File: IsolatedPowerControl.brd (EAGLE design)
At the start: 160 x 100 mm, 38 parts, among them IC1 LM358, K2 G2RATE-OJ, Q1 FDN360P, U1 MCP23008-E/SO, U2 MCP4716A0T-E/CH

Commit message: Initial fit (incomplete routing)
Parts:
- removed D2: P6KEXXCTS-P6KE, diode:DO15-10
- removed K2: G2RATE-OJ, relay:G2RA-SHORTER
- removed LED2: (no value), led:LED5MM
- removed R13: 270, rcl:R0805
- added JP1, JP3, JP6, JP7, JP8: (no value), pinhead:1X01
- JP4: device pinhead:1X07 -> pinhead:1X01
- moved D1 36.7 mm to (2.86, 38.1)
- moved Q1 35.3 mm to (18.7, 45.4), flipped to the bottom, turned to 270 degrees
- moved T3 29.3 mm to (6.35, 44.5), flipped to the bottom
- moved R14 28.4 mm to (22.2, 45.1), flipped to the bottom, turned to 270 degrees
- moved R12 19.4 mm to (12.7, 45.4), flipped to the bottom, turned to 270 degrees
- moved JP4 16.6 mm to (15.6, 36.2), turned to 0 degrees
- moved R11 12.4 mm to (9.84, 43.8), flipped to the bottom, turned to 0 degrees
- moved C6 0.63 mm to (9.53, 39.6)
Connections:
- removed net N$10: JP4.7, K2.S
- removed net N$8: LED2.K, R13.2
- removed net N$9: JP4.6, K2.P
- net DIRECTONOFF_BUFFERED: now also JP7.1; no longer JP4.5
- net N$13: now also JP8.1; no longer JP4.1
- net N$18: now also JP1.1; no longer D2.A, K2.1, R13.1
- net N$3: now also JP3.1; no longer JP4.2
- net V+: no longer D2.C, K2.2, LED2.A
- net VPOWER: now also JP4.1; no longer JP4.3
- net VPOWER_BUFFERED: now also JP6.1; no longer JP4.4
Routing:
- net DIRECTONOFF: track 0.00 -> 15.3 mm
- net V+: track 56.9 -> 69.0 mm
- net N$12: track 0.00 -> 7.44 mm
- net V-: track 12.0 -> 6.93 mm
- net N$3: track 0.00 -> 3.49 mm
- net N$18: track 0.00 -> 3.35 mm
- net FETONOFF: track 0.00 -> 2.95 mm
- net N$13: track 0.00 -> 2.79 mm
- net DIRECTONOFF_BUFFERED: track 0.65 -> 3.32 mm
- net RELAYONOFF: track 0.00 -> 2.47 mm
- net N$7: track 0.00 -> 2.36 mm
- net VPOWER: track 3.51 -> 4.07 mm

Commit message: First layout complete and checked
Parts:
- JP1, JP3, JP4, JP6, JP7, JP8: device pinhead:1X01 -> pinhead:1X01-LARGEPAD
- moved JP6 12.0 mm to (24.1, 45.7), turned to 90 degrees
- moved JP4 11.4 mm to (25.1, 42.5)
- moved C6 6.63 mm to (11.4, 46.0)
- moved R11 6.11 mm to (10.8, 49.8), turned to 90 degrees
- moved IC1 5.72 mm to (10.2, 42.5)
- moved SJ1 5.64 mm to (20.3, 40.0)
- moved T3 5.54 mm to (7.62, 49.8), turned to 270 degrees
- moved C4 5.45 mm to (7.30, 36.2)
- moved JP7 5.40 mm to (5.71, 45.1), turned to 90 degrees
- moved R14 5.40 mm to (24.8, 49.8)
- moved Q1 5.12 mm to (21.3, 49.8)
- moved JP8 4.72 mm to (16.8, 48.9), turned to 90 degrees
- moved R12 4.62 mm to (14.0, 49.8), turned to 315 degrees
- moved C7 4.49 mm to (20.6, 11.9)
- moved JP2 4.49 mm to (14.6, 31.1)
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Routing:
- net VPOWER: track 4.07 -> 17.1 mm
- net VPOWER_BUFFERED: track 0.65 -> 12.9 mm
- net GND: track 9.92 -> 0.34 mm
- net V+: track 69.0 -> 78.2 mm
- net N$12: track 7.44 -> 11.0 mm
- net V-: track 6.93 -> 4.90 mm, vias 1 -> 2
- net N$11: track 2.87 -> 4.74 mm
- net SDA: track 31.1 -> 29.3 mm
- net SCL: track 21.3 -> 22.4 mm
- net N$13: track 2.79 -> 3.74 mm
- net RY-SCL: track 9.94 -> 10.8 mm
- net RELAYONOFF: track 2.47 -> 3.28 mm
- net N$2: track 4.79 -> 4.07 mm
- net DIRECTONOFF: track 15.3 -> 14.7 mm
- net N$5: track 7.95 -> 7.37 mm, vias 2 -> 1
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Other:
- board size 160 x 100 mm -> 27.9 x 53.6 mm

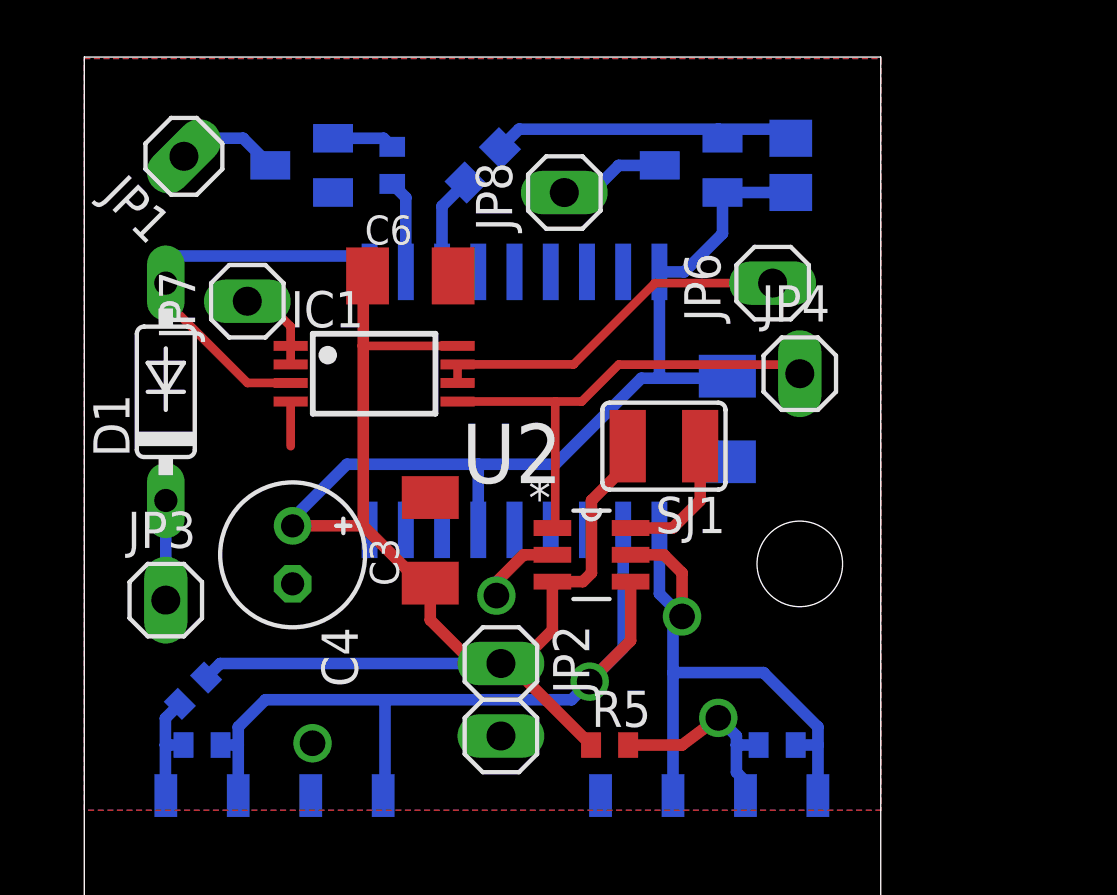
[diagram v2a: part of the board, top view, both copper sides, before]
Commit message: Added op amp with enable/power down (MCP6273T) and re-routed.
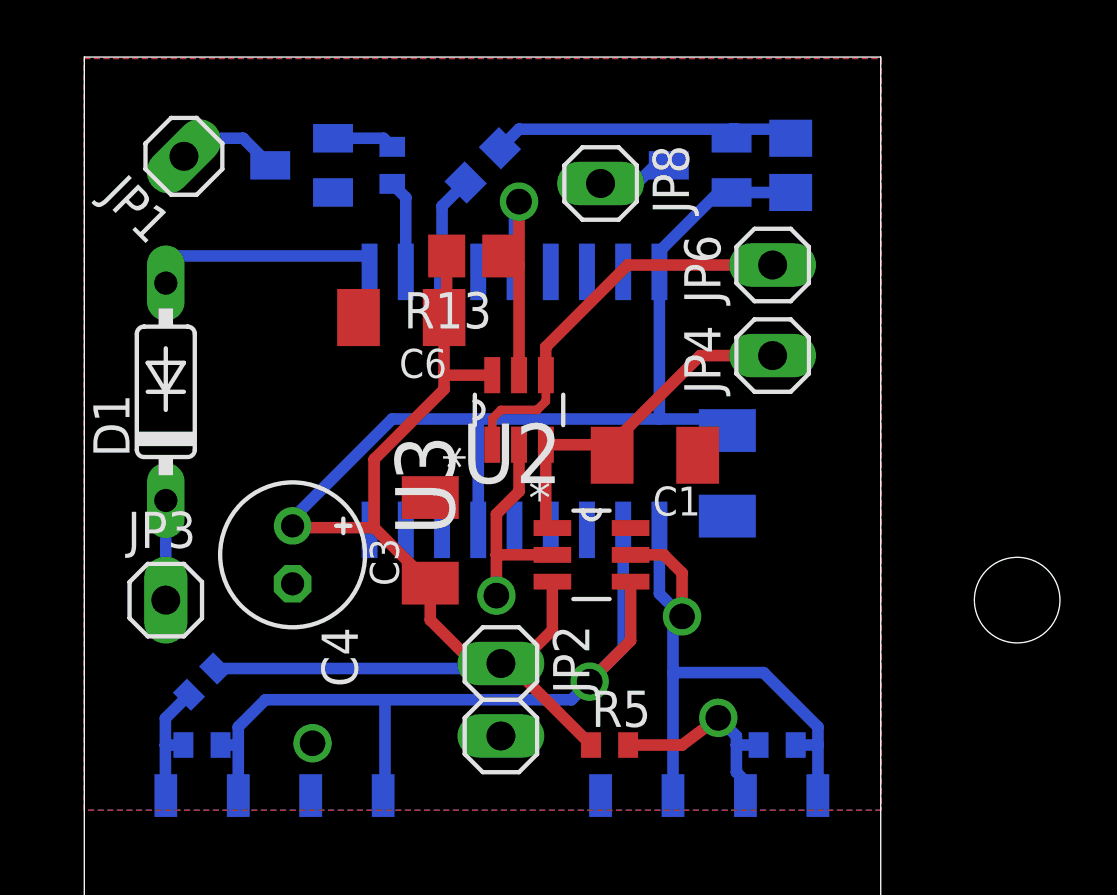
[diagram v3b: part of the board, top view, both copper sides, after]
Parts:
- removed IC1: LM358, linear:TSSOP8
- removed JP7: (no value), pinhead:1X01-LARGEPAD
- removed SJ1: (no value), jumper:SJW
- added C1: 100n, rcl:C1206K
- added R13: 10K, rcl:R0805
- added U3: MCP6273T-E/CH, MCP6273T-ECH:SOT95P280X145-6N
- moved C2 1.91 mm to (22.5, 39.1)
- moved C6 1.49 mm to (11.1, 44.5), turned to 180 degrees
- moved JP8 1.31 mm to (18.1, 49.2), turned to 270 degrees
- moved JP4 1.14 mm to (24.1, 43.2), turned to 90 degrees
- moved JP6 0.63 mm to (24.1, 46.4)
- moved R9 0.45 mm to (4.13, 31.8)
- moved Q1 0.32 mm to (21.6, 49.8)
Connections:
- removed net DIRECTONOFF_BUFFERED: IC1.1, IC1.2, JP7.1
- removed net N$11: SJ1.1, U2.6
- new net POWERSHUTDOWN_N: R13.1, U1.14, U3.5
- net DIRECTONOFF: no longer IC1.3
- net V+: now also R13.2, U3.6; no longer IC1.8, SJ1.2
- net V-: now also C1.1, U3.2; no longer IC1.4
- net VPOWER: now also C1.2, U3.3; no longer IC1.5
- net VPOWER_BUFFERED: now also U3.1, U3.4; no longer IC1.6, IC1.7
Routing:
- net POWERSHUTDOWN_N: track 0.00 -> 9.47 mm, vias 0 -> 1
- net DIRECTONOFF: track 14.7 -> 8.47 mm
- net V+: track 78.2 -> 73.3 mm
- net N$11: track 4.74 -> 0.00 mm
- net VPOWER: track 17.1 -> 13.2 mm
- net DIRECTONOFF_BUFFERED: track 3.22 -> 0.00 mm
- net V-: track 4.90 -> 8.08 mm
- net VPOWER_BUFFERED: track 12.9 -> 14.1 mm
- net N$13: track 3.74 -> 2.66 mm

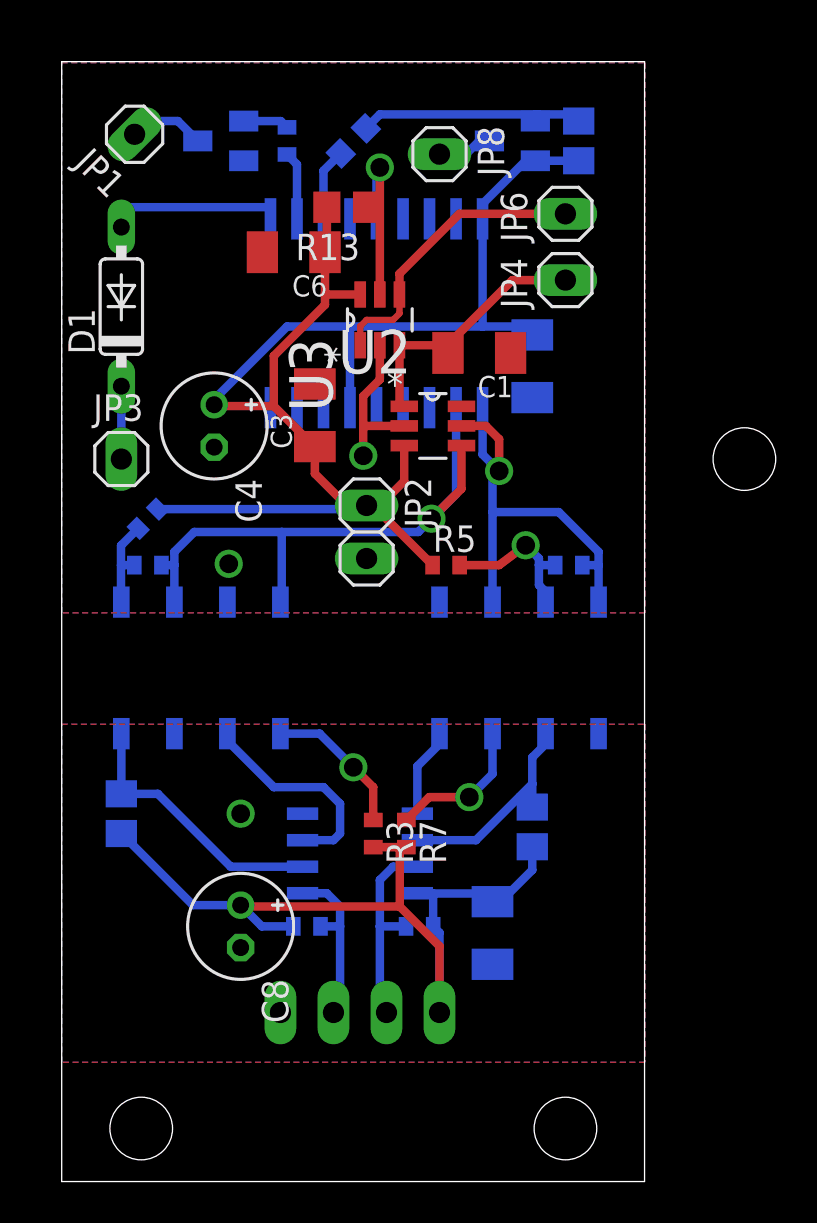
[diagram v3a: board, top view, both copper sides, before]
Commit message: Added another isolated aux channel
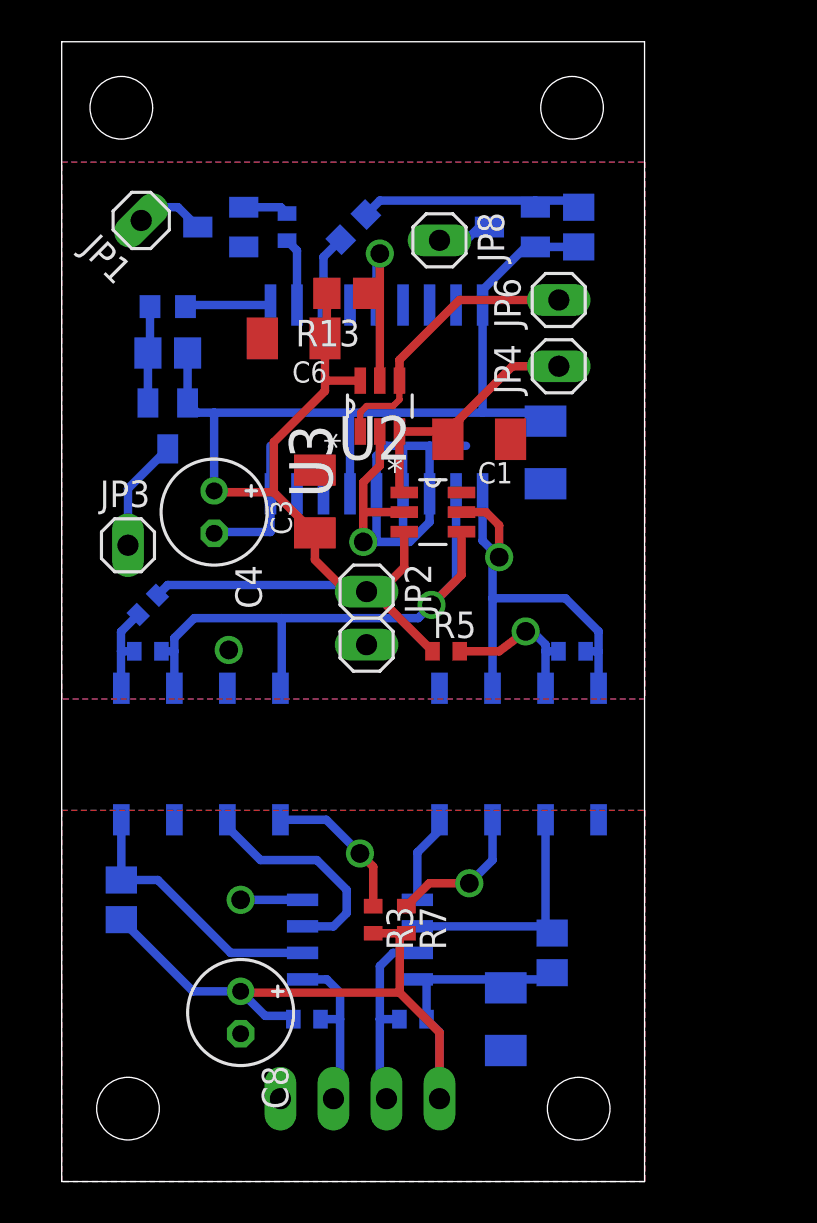
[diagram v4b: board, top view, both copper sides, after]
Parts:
- removed D1: 1N4148DO35-7, diode:DO35-7
- added Q2: FDN340P, transistor-power:SUPER-SOT3
- added R15: 10, rcl:R0603
- added R16: 10K, rcl:R0805
- Q1: value FDN360P -> FDN340P
- moved R2 6.11 mm to (23.5, 11.0)
- moved R1 4.46 mm to (16.8, 7.78)
- moved R10 4.45 mm to (11.7, 7.78)
- moved C2 4.18 mm to (23.2, 34.9)
- moved C7 4.18 mm to (21.3, 7.78)
- moved JP3 4.14 mm to (3.17, 30.5)
- moved JP1 4.14 mm to (3.81, 46.0)
- moved JP4 4.14 mm to (23.8, 39.1)
- moved JP6 4.14 mm to (23.8, 42.2)
- moved R4 4.13 mm to (24.4, 25.4)
- moved C3 4.13 mm to (12.1, 32.6)
- moved C8 4.13 mm to (8.57, 8.10)
- moved R5 4.13 mm to (18.4, 25.4)
- moved R8 4.13 mm to (4.13, 25.4)
- moved R9 4.13 mm to (4.13, 27.6)
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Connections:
- net FETONOFF renamed HIGHSIDEONOFF_A
- net N$13 renamed SWITCHEDV+A
- net N$18 renamed SWITCHEDV-A
- net RELAYONOFF renamed LOWSIDEONOFF_A
- removed net DIRECTONOFF: D1.A, U1.10
- removed net N$3: D1.C, JP3.1
- new net HIGHSIDEONOFF_B: R15.2, U1.10
- new net N$8: Q2.1, R15.1, R16.1
- new net SWITCHEDV+B: JP3.1, Q2.3
- net V+: now also Q2.2, R16.2
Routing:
- net V-: track 8.08 -> 35.3 mm
- net DIRECTONOFF: track 8.47 -> 0.00 mm
- net V+: track 73.3 -> 80.3 mm
- net SWITCHEDV+B: track 0.00 -> 5.40 mm
- net N$8: track 0.00 -> 4.66 mm
- net HIGHSIDEONOFF_B: track 0.00 -> 4.10 mm
- net N$3: track 3.49 -> 0.00 mm
- net GND: track 0.34 -> 3.31 mm
- net RY-SCL: track 10.8 -> 11.9 mm
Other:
- board size 27.9 x 53.6 mm -> 27.9 x 54.6 mm

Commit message: Another reroute!
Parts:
- moved JP1 20.0 mm to (23.8, 46.4), turned to 90 degrees
- moved Q1 14.9 mm to (6.67, 45.7)
- moved JP8 14.6 mm to (3.49, 45.7), turned to 0 degrees
- moved R14 14.6 mm to (10.2, 45.7)
- moved T3 12.4 mm to (20.0, 46.7), turned to 90 degrees
- moved R11 9.03 mm to (19.7, 44.1), turned to 180 degrees
- moved R13 4.62 mm to (9.21, 43.8)
- moved U3 3.43 mm to (13.3, 40.0)
- moved U2 2.86 mm to (17.8, 34.9), turned to 315 degrees
- moved C3 2.43 mm to (13.8, 34.4), turned to 135 degrees
- moved C6 1.89 mm to (9.78, 39.1), turned to 270 degrees
- moved JP3 1.59 mm to (3.17, 32.1)
- moved C1 1.59 mm to (20.0, 37.1), turned to 135 degrees
- moved R12 1.27 mm to (12.7, 45.7), turned to 270 degrees
- moved JP4 0.32 mm to (23.8, 38.7)
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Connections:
- net LOWSIDEONOFF_A: now also U1.17; no longer U1.11
- net V+: now also U1.11
- net V-: now also U1.15, U1.16
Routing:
- net V+: track 80.3 -> 94.0 mm
- net V-: track 35.3 -> 42.5 mm
- net N$12: track 10.9 -> 5.03 mm
- net SCL: track 22.4 -> 25.7 mm
- net POWERSHUTDOWN_N: track 9.47 -> 12.2 mm
- net SWITCHEDV+B: track 5.40 -> 3.82 mm
- net VPOWER: track 12.8 -> 11.5 mm
- net LOWSIDEONOFF_A: track 3.28 -> 2.29 mm
- net N$5: track 7.40 -> 8.38 mm
- net SDA: track 29.3 -> 28.6 mm
- net SWITCHEDV+A: track 2.66 -> 2.07 mm
- net SWITCHEDV-A: track 3.37 -> 2.84 mm
- net HIGHSIDEONOFF_A: track 3.48 -> 2.95 mm
